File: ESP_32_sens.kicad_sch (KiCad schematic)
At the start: 0 parts

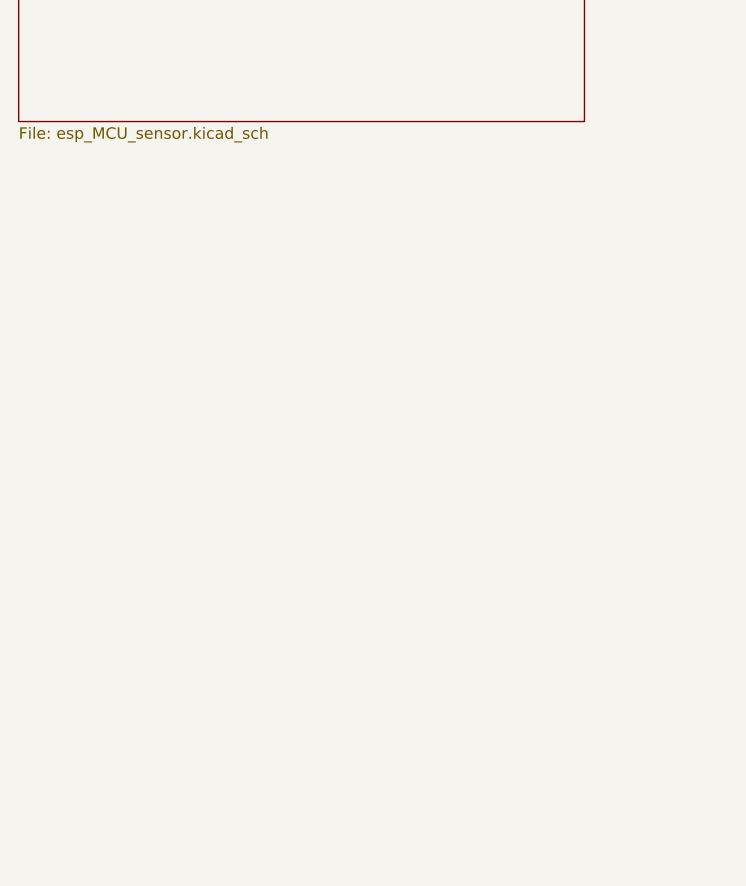
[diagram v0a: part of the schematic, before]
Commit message: Add RF schematics for GPS + designed Pi filter for imp matching
added impedance matching on LNA 1 pin, added GPS/GNSS IC
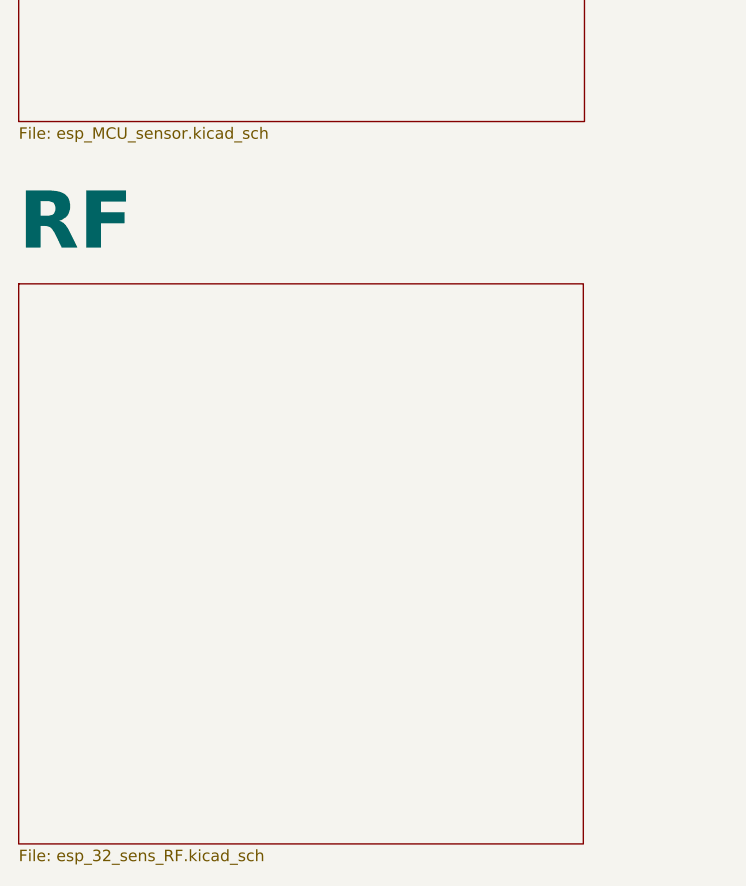
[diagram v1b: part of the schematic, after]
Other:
- added sheet RF (esp_32_sens_RF.kicad_sch)
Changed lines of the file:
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@@
+		)
+	)
+	(sheet
+		(at 38.1 101.854)
+		(size 62.738 62.23)
+		(exclude_from_sim no)
+		(in_bom yes)
+		(on_board yes)
+		(dnp no)
+		(fields_autoplaced yes)
+		(stroke
+			(width 0.1524)
+			(type solid)
+		)
+		(fill
+			(color 0 0 0 0.0000)
+		)
+		(property "Sheetname" "RF"
+			(at 38.1 98.6024 0)
+			(effects
+				(font
+					(face "KiCad Font")
+					(size 6.35 6.35)
+					(thickness 1.27)
+					(bold yes)
+				)
+				(justify left bottom)
+			)
+		)
+		(property "Sheetfile" "esp_32_sens_RF.kicad_sch"
+			(at 38.1 164.6686 0)
+			(effects
+				(font
+					(size 1.27 1.27)
+				)
+				(justify left top)
+			)
+		)
+		(instances
+			(project "ESP_32_sens"
+				(path "/185194d2-a1d5-42f3-9012-92a466d7f7ac"
+					(page "4")
+				)
+			)
 		)
 	)

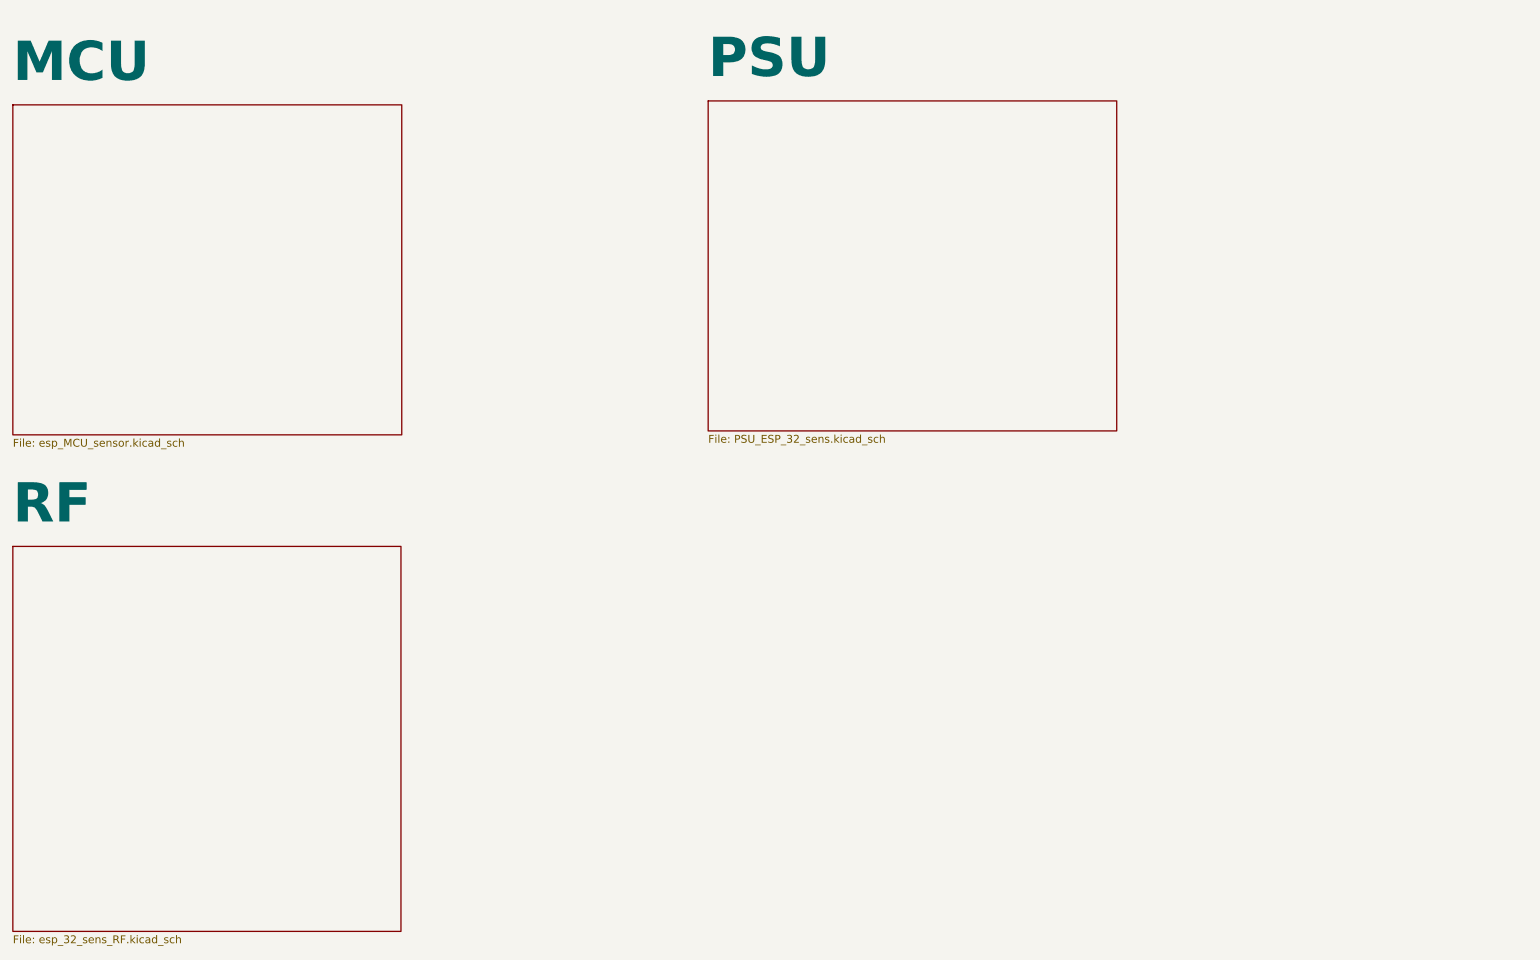
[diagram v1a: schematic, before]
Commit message: placement done
placement done, routing left
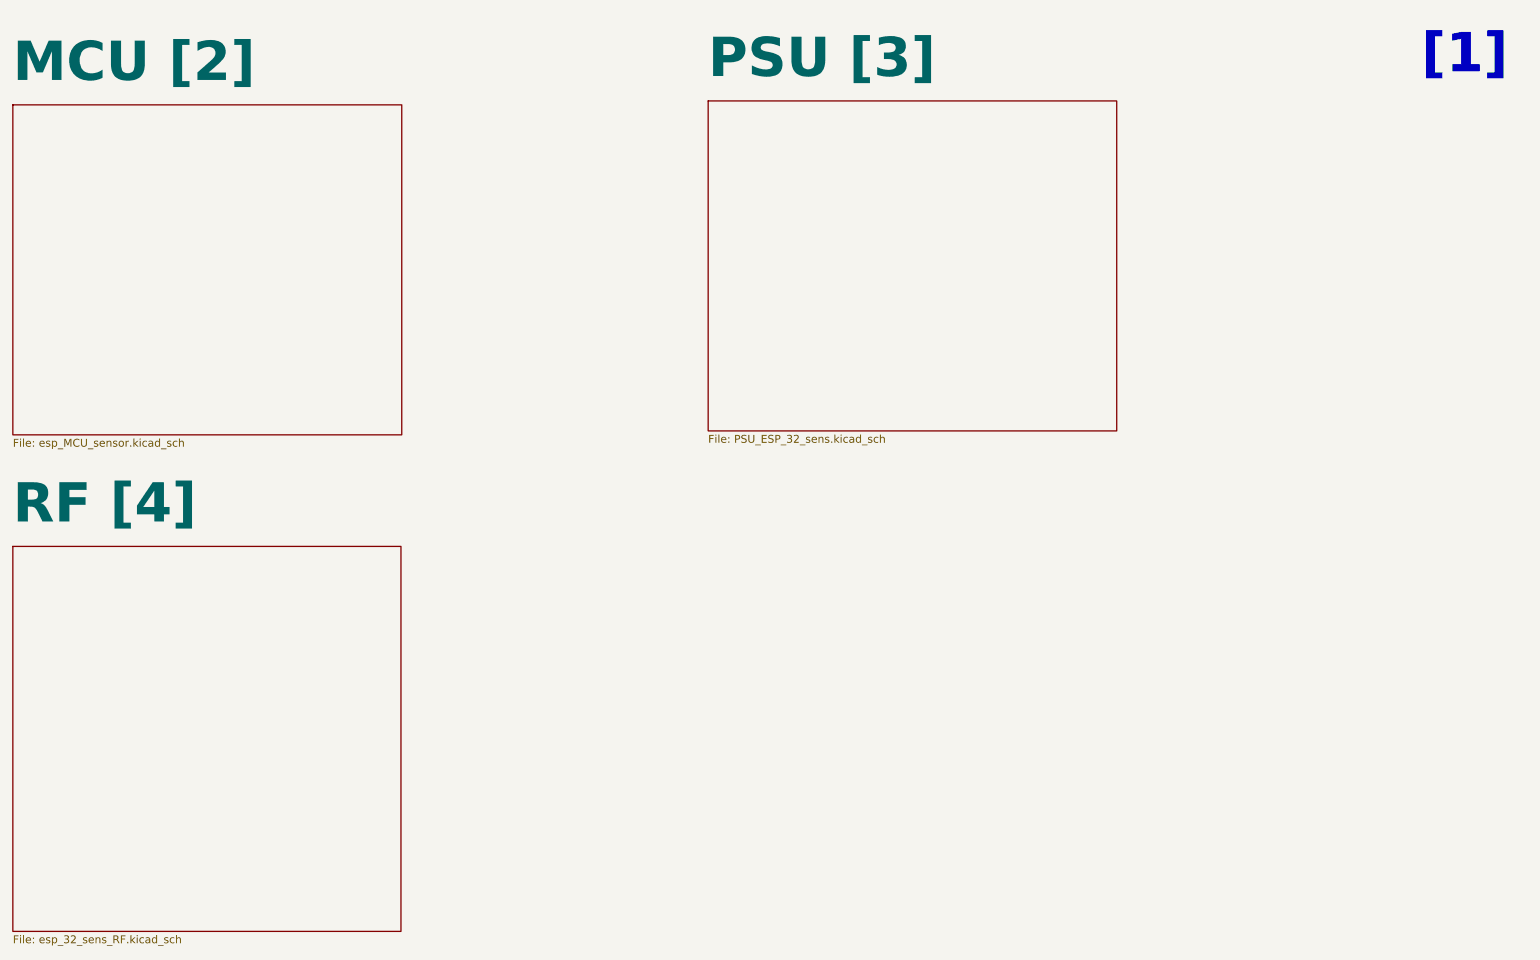
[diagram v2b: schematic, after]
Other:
- sheet MCU renamed MCU [2]
- sheet PSU renamed PSU [3]
- sheet RF renamed RF [4]
- note added: "[1]"
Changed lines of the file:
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@@
 		(title "Motion_Tracker_V0")
+	)
+	(text "[1]"
+		(exclude_from_sim no)
+		(at 272.796 22.352 0)
+		(effects
+			(font
+				(size 6.35 6.35)
+				(thickness 1.27)
+				(bold yes)
+			)
+		)
 	)
 	(sheet
@@
 			(color 0 0 0 0.0000)
 		)
-		(property "Sheetname" "PSU"
+		(property "Sheetname" "PSU [3]"
 			(at 150.495 26.5934 0)
 			(effects
@@
 			(color 0 0 0 0.0000)
 		)
-		(property "Sheetname" "MCU"
+		(property "Sheetname" "MCU [2]"
 			(at 38.1 27.2284 0)
 			(effects
@@
 			(color 0 0 0 0.0000)
 		)
-		(property "Sheetname" "RF"
+		(property "Sheetname" "RF [4]"
 			(at 38.1 98.6024 0)
 			(effects
